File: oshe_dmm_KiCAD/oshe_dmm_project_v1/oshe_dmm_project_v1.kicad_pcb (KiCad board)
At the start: 4 copper layers, 101.6 x 177.8 mm, 55 parts, among them J1 FTDI Basic, J2 USB_C_Receptacle_PowerOnly_6P, J3 ON/OFF, SW1 SW_Push, U1 ATmega328P-A, U2 INA219BxD, U3 BQ24075RGT, U4 LM317_SOT-223, Y1 16MHz

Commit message: More changes plus custom footprints and symbols!
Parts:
- added F1: 5A, Fuse:Fuseholder_Clip-5x20mm_Keystone_3512P_Inline_P23.62x7.27mm_D1.02x2.41x1.02x1.57mm_Horizontal, F.Cu at (176.8, 235.1)
- F2: renamed from F1; value Fuse -> 500mA
- SW1: value SW_Push -> PTS526 SK15 SMTR2 LFS; footprint Button_Switch_SMD:SW_Push_1P1T-MP_NO_Horizontal_Alps_SKRTLAE010 -> DMM_Footprint_Library:SMT_FS
- moved D1 8.52 mm to (189.3, 217.0)
- moved R2 8.52 mm to (190.8, 206.8)
- moved R3 8.52 mm to (189.3, 210.6)
- moved SW1 8.47 mm to (131.1, 175.6)
- moved F2 8.26 mm to (197.9, 223.3)
- moved R1 2.67 mm to (170.8, 232.8)
- moved R4 2.67 mm to (154.5, 232.5)
- moved C2 2.67 mm to (166.5, 235.6)
- moved R5 2.67 mm to (154.5, 230.1)
- moved U2 2.67 mm to (161.4, 233.1)
- renumbered C10 to C12, C11 to C13, C12 to C15, C13 to C16, R2 to R1, R9 to R14, R10 to R15, R11 to R16, R12 to R19, R1 to R2, R14 to R20, R13 to R21, R4 to R3, R3 to R4, R8 to R9, RV2 to RV1, U4 to U5
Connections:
- net Current Positive renamed Net-(U2-IN+)
- DS1 pad 15: +5V -> Net-(DS1-LED(+))
- SW1 pad 1: GND -> Net-(U1-~{RESET}/PC6)
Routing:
- net GND: track 22.2 -> 36.6 mm
- net Net-(U1-~{RESET}/PC6): track 49.0 -> 59.4 mm

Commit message: Friday Library Meeting
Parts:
- added C14: 100nF, Capacitor_SMD:C_1206_3216Metric_Pad1.33x1.80mm_HandSolder, F.Cu at (94.3, 133.3)
- added D6: SMAJ200CA, Diode_SMD:D_SMA, F.Cu at (79.0, 114.3)
- added J4: Voltage, DMM_Footprint_Library:CONN_575-8_KEY, F.Cu at (207.5, 192.3)
- added J5: GND, DMM_Footprint_Library:CONN_575-8_KEY, F.Cu at (207.5, 211.3)
- added J6: Current, DMM_Footprint_Library:CONN_575-8_KEY, F.Cu at (207.5, 230.3)
- added R10: 900K, Resistor_SMD:R_1206_3216Metric_Pad1.30x1.75mm_HandSolder, F.Cu at (192.9, 151.2)
- added R11: 90k, Resistor_SMD:R_1206_3216Metric_Pad1.30x1.75mm_HandSolder, F.Cu at (192.9, 156.6)
- added R13: 10k, Resistor_SMD:R_1206_3216Metric_Pad1.30x1.75mm_HandSolder, F.Cu at (192.9, 162.0)
- added R22: 10k, Resistor_SMD:R_1206_3216Metric_Pad1.30x1.75mm_HandSolder, F.Cu at (100.8, 129.0)
- added R23: 10k, Resistor_SMD:R_1206_3216Metric_Pad1.30x1.75mm_HandSolder, F.Cu at (100.8, 131.4)
- added R8: 220K, Resistor_SMD:R_1206_3216Metric_Pad1.30x1.75mm_HandSolder, F.Cu at (127.4, 138.1)
- added U6: ADS1115IDGS, Package_SO:TSSOP-10_3x3mm_P0.5mm, F.Cu at (89.0, 131.8)
- moved F2 40.3 mm to (207.5, 184.2)
- moved F1 19.8 mm to (196.6, 234.9), turned to 180 degrees
- moved C2 7.38 mm to (167.0, 228.3)
- moved R5 7.38 mm to (155.0, 222.7)
- moved U2 7.38 mm to (161.9, 225.7)
- moved R1 7.38 mm to (171.3, 225.5)
- moved R4 7.38 mm to (155.0, 225.1)
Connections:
- net Current Negative renamed Input_Negative
- F1 pad 1: Current Positive -> Current_Input
- F2 pad 1: Net-(F2-Pad1) -> Voltage_Input
- F2 pad 2: Net-(F2-Pad2) -> /2V
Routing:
- net /2V: track 0.00 -> 29.8 mm
- net Voltage_Input: track 0.00 -> 8.10 mm
- net (no net): vias 0 -> 1
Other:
- outline, holes or cut-outs redrawn

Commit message: Replaced PCB file with update
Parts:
- moved R10 3.40 mm to (196.3, 151.5)
- moved R11 3.40 mm to (196.3, 156.9)
- moved R13 3.40 mm to (196.3, 162.4)
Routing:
- net /2V: track 29.8 -> 31.3 mm
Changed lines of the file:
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@@
 		(fp_arc
 			(start 64.20104 22.49932)
-			(mid 64.054473 22.853115)
+			(mid 64.054479 22.85315)
 			(end 63.70066 22.9997)
 			(stroke
@@
 	(footprint "Resistor_SMD:R_1206_3216Metric_Pad1.30x1.75mm_HandSolder"
 		(layer "F.Cu")
-		(at 192.93 162.048 -90)
+		(at 196.315 162.389 -90)
 		(descr "Resistor SMD 1206 (3216 Metric), square (rectangular) end terminal, IPC_7351 nominal with elongated pad for handsoldering. (Body size source: IPC-SM-782 page 72, https://www.pcb-3d.com/wordpress/wp-content/uploads/ipc-sm-782a_amendment_1_and_2.pdf), generated with kicad-footprint-generator")
 		(tags "resistor handsolder")
@@
 		(tags "resistor handsolder")
 		(property "Reference" "R23"
-			(at -3.937 0 360)
+			(at -3.937 0 0)
 			(layer "F.SilkS")
 			(effects
@@
 		)
 		(property "Value" "10k"
-			(at 0 1.82 360)
+			(at 0 1.82 0)
 			(layer "F.Fab")
 			(effects
@@
 		)
 		(fp_text user "${REFERENCE}"
-			(at 0 0 360)
+			(at 0 0 0)
 			(layer "F.Fab")
 			(effects
@@
 		(tags "fuse clip open")
 		(property "Reference" "F1"
-			(at 11.81 -4.5 360)
+			(at 11.81 -4.5 0)
 			(layer "F.SilkS")
 			(effects
@@
 		)
 		(property "Value" "5A"
-			(at 11.555 4.5 360)
+			(at 11.555 4.5 0)
 			(layer "F.Fab")
 			(effects
@@
 		)
 		(fp_text user "${REFERENCE}"
-			(at 11.81 0 360)
+			(at 11.81 0 0)
 			(layer "F.Fab")
 			(effects
@@
 	(footprint "Resistor_SMD:R_1206_3216Metric_Pad1.30x1.75mm_HandSolder"
 		(layer "F.Cu")
-		(at 192.93 151.15 -90)
+		(at 196.315 151.491 -90)
 		(descr "Resistor SMD 1206 (3216 Metric), square (rectangular) end terminal, IPC_7351 nominal with elongated pad for handsoldering. (Body size source: IPC-SM-782 page 72, https://www.pcb-3d.com/wordpress/wp-content/uploads/ipc-sm-782a_amendment_1_and_2.pdf), generated with kicad-footprint-generator")
 		(tags "resistor handsolder")
@@
 	(footprint "Resistor_SMD:R_1206_3216Metric_Pad1.30x1.75mm_HandSolder"
 		(layer "F.Cu")
-		(at 192.93 156.587 -90)
+		(at 196.315 156.928 -90)
 		(descr "Resistor SMD 1206 (3216 Metric), square (rectangular) end terminal, IPC_7351 nominal with elongated pad for handsoldering. (Body size source: IPC-SM-782 page 72, https://www.pcb-3d.com/wordpress/wp-content/uploads/ipc-sm-782a_amendment_1_and_2.pdf), generated with kicad-footprint-generator")
 		(tags "resistor handsolder")
@@
 		(tags "resistor handsolder")
 		(property "Reference" "R22"
-			(at -3.937 0 360)
+			(at -3.937 0 0)
 			(layer "F.SilkS")
 			(effects
@@
 		)
 		(property "Value" "10k"
-			(at 0 1.82 360)
+			(at 0 1.82 0)
 			(layer "F.Fab")
 			(effects
@@
 		)
 		(fp_text user "${REFERENCE}"
-			(at 0 0 360)
+			(at 0 0 0)
 			(layer "F.Fab")
 			(effects
@@
 	(gr_circle
 		(center 164.49 152.078)
-		(end 174.49 152.078)
+		(end 189.490112 152.078)
 		(stroke
 			(width 2)
@@
 	(gr_circle
 		(center 164.49 152.078)
-		(end 179.49 152.078)
+		(end 174.49 152.078)
 		(stroke
 			(width 2)
@@
 	(gr_circle
 		(center 164.49 152.078)
-		(end 184.49 152.078)
+		(end 179.49 152.078)
 		(stroke
 			(width 2)
@@
 		(layer "F.Cu")
 	)
+	(gr_arc
+		(start 171.355591 133.293334)
+		(mid 174.515111 134.772014)
+		(end 177.36964 136.777187)
+		(stroke
+			(width 2)
+			(type default)
+		)
+		(layer "F.Cu")
+	)
+	(gr_arc
+		(start 184.19146 148.63527)
+		(mid 184.489977 152.107139)
+		(end 184.181345 155.578124)
+		(stroke
+			(width 2)
+			(type default)
+		)
+		(layer "F.Cu")
+	)
+	(gr_arc
+		(start 179.834186 139.250063)
+		(mid 181.825381 142.103805)
+		(end 183.291804 145.259484)
+		(stroke
+			(width 2)
+			(type default)
+		)
+		(layer "F.Cu")
+	)
 	(gr_line
 		(start 148.488 240.47)
@@
 	)
 	(gr_arc
-		(start 150.389743 146.959687)
-		(mid 151.493044 144.58844)
-		(end 152.991432 142.444865)
+		(start 171.355591 133.293334)
+		(mid 174.515111 134.772014)
+		(end 177.36964 136.777187)
 		(stroke
-			(width 0.1)
+			(width 2)
 			(type default)
 		)
@@
 	)
 	(gr_arc
-		(start 167.092897 137.305071)
-		(mid 167.734534 137.432608)
-		(end 168.37 137.588)
+		(start 164.49 132.078)
+		(mid 166.238117 132.154544)
+		(end 167.972853 132.383591)
 		(stroke
 			(width 0.5)
@@
 	)
 	(gr_arc
-		(start 154.840216 140.593398)
-		(mid 156.983677 139.090717)
-		(end 159.355732 137.983544)
+		(start 167.972853 132.383591)
+		(mid 169.684178 132.764261)
+		(end 171.355591 133.293334)
 		(stroke
-			(width 0.1)
+			(width 0.5)
 			(type default)
 		)
@@
 	)
 	(gr_arc
-		(start 174.127591 140.583164)
-		(mid 175.090932 141.465053)
-		(end 175.973912 142.427394)
+		(start 168.37 137.588)
+		(mid 164.495001 167.078482)
+		(end 160.600343 137.59059)
 		(stroke
-			(width 0.5)
+			(width 2)
 			(type default)
 		)
@@
 	)
 	(gr_arc
-		(start 152.991431 142.444864)
-		(mid 153.875378 141.478745)
-		(end 154.840216 140.593398)
+		(start 168.837468 127.458911)
+		(mid 170.975549 127.933898)
+		(end 173.063852 128.594196)
 		(stroke
 			(width 0.5)
@@
 	)
 	(gr_arc
-		(start 168.37 137.588)
-		(mid 168.998655 137.77113)
-		(end 169.618719 137.981521)
+		(start 167.08526 142.420641)
+		(mid 167.505215 142.543409)
+		(end 167.919399 142.684428)
 		(stroke
-			(width 0.5)
+			(width 0.1)
 			(type default)
 		)
@@
 	)
 	(gr_arc
-		(start 178.582584 146.938592)
-		(mid 178.977173 148.187465)
-		(end 179.261319 149.465998)
+		(start 173.063852 128.594197)
+		(mid 186.151091 139.59613)
+		(end 189.107234 156.435951)
 		(stroke
-			(width 0.5)
+			(width 2)
 			(type default)
 		)
@@
 	)
 	(gr_arc
-		(start 161.884844 137.30547)
-		(mid 164.488853 137.077517)
-		(end 167.092897 137.305071)
+		(start 151.642701 136.750023)
+		(mid 154.496384 134.753809)
+		(end 157.653083 133.28288)
 		(stroke
 			(width 0.1)
@@
 	)
 	(gr_arc
-		(start 179.261318 149.465998)
-		(mid 179.490478 152.070528)
-		(end 179.263913 154.675286)
+		(start 184.19146 148.63527)
+		(mid 184.489977 152.107139)
+		(end 184.181345 155.578124)
+		(stroke
+			(width 2)
+			(type default)
+		)
+		(layer "F.Mask")
+	)
+	(gr_arc
+		(start 161.030142 132.379539)
+		(mid 162.753513 132.153527)
+		(end 164.49 132.078)
+		(stroke
+			(width 0.5)
+			(type default)
+		)
+		(layer "F.Mask")
+	)
+	(gr_arc
+		(start 179.834186 139.250063)
+		(mid 181.825381 142.103805)
+		(end 183.291804 145.259484)
+		(stroke
+			(width 2)
+			(type default)
+		)
+		(layer "F.Mask")
+	)
+	(gr_arc
+		(start 145.693403 145.245149)
+		(mid 147.169742 142.07757)
+		(end 149.174918 139.215333)
 		(stroke
 			(width 0.1)
@@
 	)
 	(gr_arc
-		(start 159.355732 137.983543)
-		(mid 159.973762 137.773525)
-		(end 160.600343 137.590592)
+		(start 157.653083 133.28288)
+		(mid 159.321838 132.757284)
+		(end 161.030142 132.37954)
 		(stroke
 			(width 0.5)
@@
 	)
 	(gr_arc
-		(start 169.618719 137.981522)
-		(mid 171.986874 139.085258)
-		(end 174.127592 140.583163)
+		(start 167.919399 142.684429)
+		(mid 164.486833 162.077995)
+		(end 161.066551 142.682259)
 		(stroke
-			(width 0.1)
+			(width 2)
 			(type default)
 		)
@@
 	)
 	(gr_arc
-		(start 160.600343 137.590591)
-		(mid 161.239466 137.433941)
-		(end 161.884844 137.305471)
+		(start 149.174918 139.215333)
+		(mid 150.35496 137.928774)
+		(end 151.642701 136.750023)
 		(stroke
 			(width 0.5)
@@
 	)
 	(gr_arc
-		(start 175.973912 142.427394)
-		(mid 177.475646 144.568844)
-		(end 178.582584 146.938592)
+		(start 164.49 127.078)
+		(mid 166.672062 127.17341)
+		(end 168.837468 127.458911)
 		(stroke
-			(width 0.1)
+			(width 0.5)
 			(type default)
 		)
@@
 	)
 	(segment
+		(start 209.054 162.803)
+		(end 185.739 162.803)
+		(width 0.2)
+		(layer "B.Cu")
+		(net 60)
+	)
+	(segment
 		(start 180.48 160.588)
 		(end 178.569264 158.677264)
@@
 	)
 	(segment
-		(start 207.543 160.588)
-		(end 180.48 160.588)
+		(start 210.928 160.929)
+		(end 209.054 162.803)
+		(width 0.2)
+		(layer "B.Cu")
+		(net 60)
+	)
+	(segment
+		(start 185.739 162.803)
+		(end 183.865 160.929)
 		(width 0.2)
 		(layer "B.Cu")

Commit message: updated
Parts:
- moved R10 3.31 mm to (198.5, 149.0)
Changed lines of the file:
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@@
 		(fp_arc
 			(start 64.20104 22.49932)
-			(mid 64.054479 22.85315)
+			(mid 64.054473 22.853115)
 			(end 63.70066 22.9997)
 			(stroke
@@
 	(footprint "Resistor_SMD:R_1206_3216Metric_Pad1.30x1.75mm_HandSolder"
 		(layer "F.Cu")
-		(at 196.315 151.491 -90)
+		(at 198.465 148.978 -90)
 		(descr "Resistor SMD 1206 (3216 Metric), square (rectangular) end terminal, IPC_7351 nominal with elongated pad for handsoldering. (Body size source: IPC-SM-782 page 72, https://www.pcb-3d.com/wordpress/wp-content/uploads/ipc-sm-782a_amendment_1_and_2.pdf), generated with kicad-footprint-generator")
 		(tags "resistor handsolder")

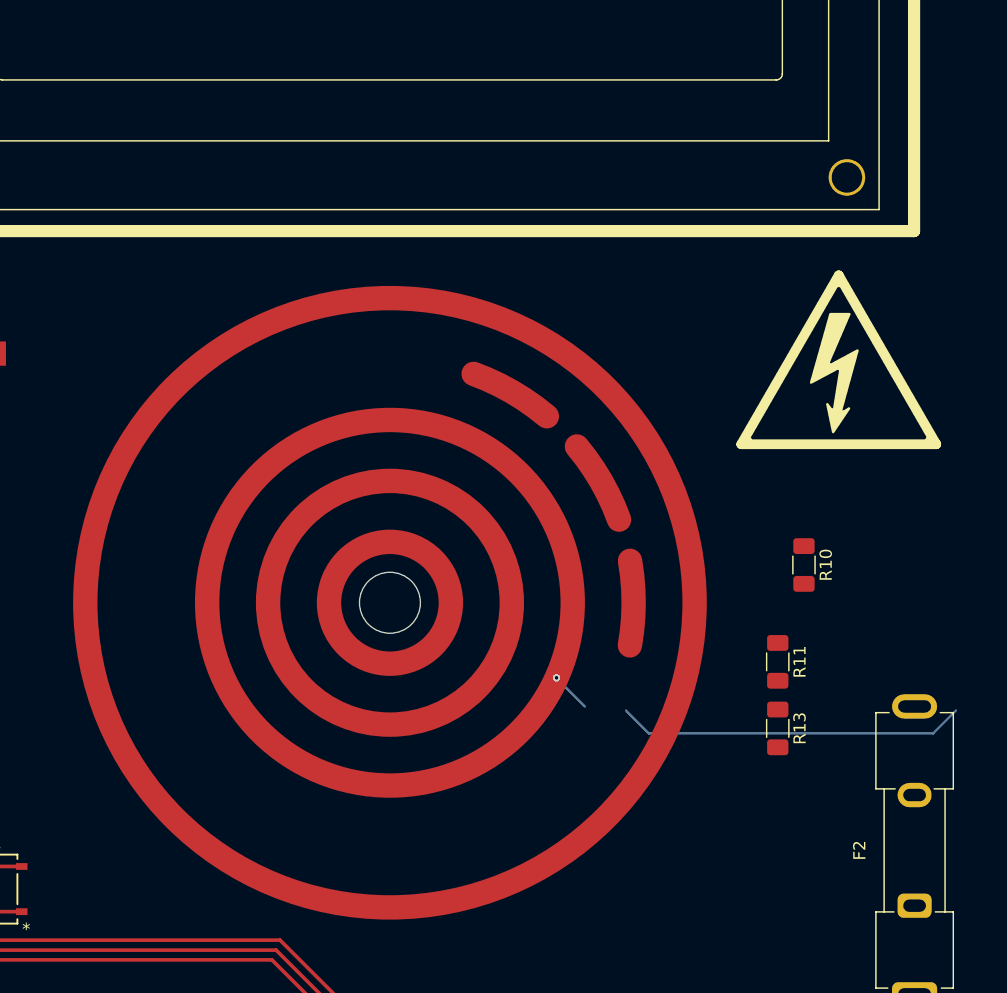
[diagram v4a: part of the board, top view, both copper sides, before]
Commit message: Updated Switch
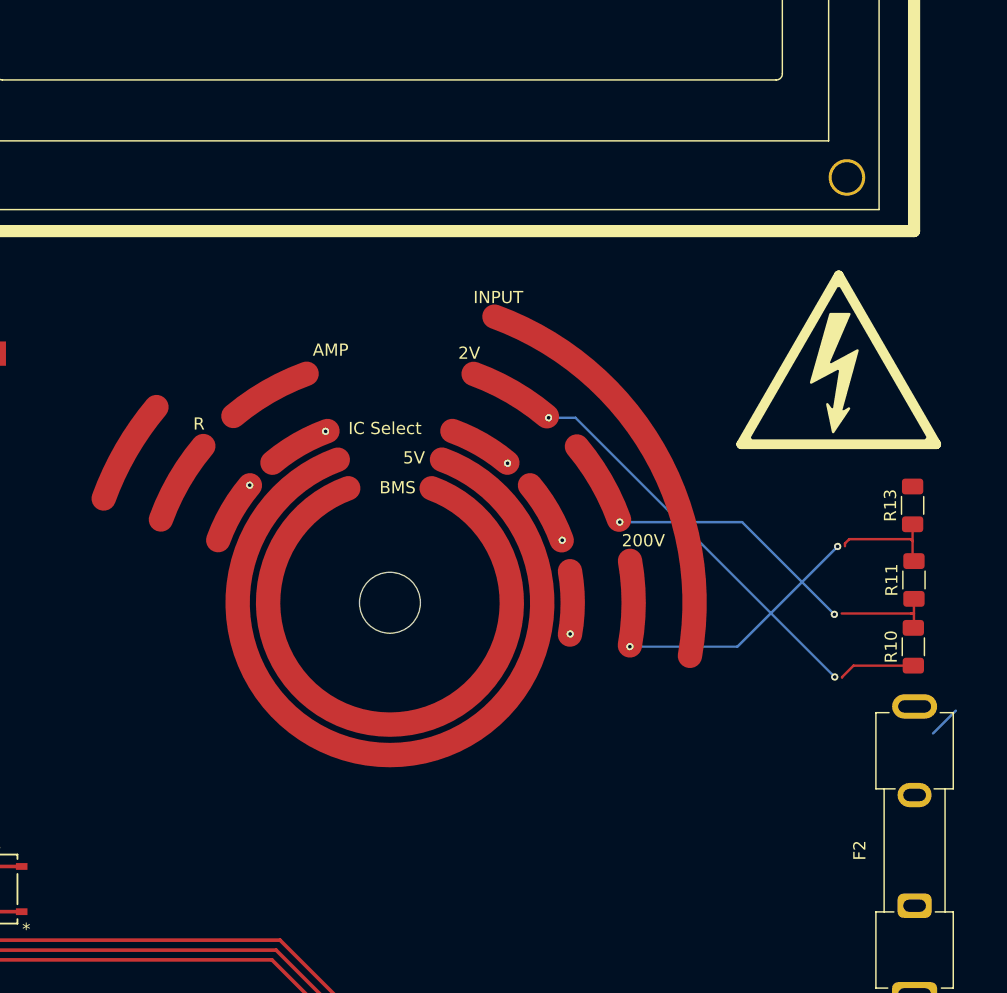
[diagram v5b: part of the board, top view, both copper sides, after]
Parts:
- moved R13 21.4 mm to (207.4, 144.1), turned to 90 degrees
- moved R11 13.0 mm to (207.5, 150.2), turned to 90 degrees
- moved R10 11.2 mm to (207.4, 155.7), turned to 90 degrees
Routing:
- net (no net): track 0.00 -> 73.5 mm, vias 1 -> 11
- net /2V: track 31.3 -> 8.93 mm
- net /200V: track 0.00 -> 9.06 mm
- net /20V: track 0.00 -> 8.33 mm
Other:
- board text added: "200V"
- board text added: "20V"
- board text added: "2V"
- board text added: "AMP"
- board text added: "BMS"
- board text added: "IC Select"
- board text added: "INPUT"
- board text added: "R"

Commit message: Made some updates
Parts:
- removed C14: 100nF, Capacitor_SMD:C_1206_3216Metric_Pad1.33x1.80mm_HandSolder
- removed the D1 at (189.3, 217.0)
- removed the R2 at (190.8, 206.8)
- added C11: 0.1uF, Capacitor_SMD:C_1206_3216Metric_Pad1.33x1.80mm_HandSolder, F.Cu at (181.6, 197.7)
- added J10: Voltage Range 2, Connector_PinHeader_2.54mm:PinHeader_1x02_P2.54mm_Vertical, F.Cu at (202.5, 136.5)
- added J11: Voltage Range 3, Connector_PinHeader_2.54mm:PinHeader_1x02_P2.54mm_Vertical, F.Cu at (197.8, 144.6)
- added J12: Voltage Range 3, Connector_PinHeader_2.54mm:PinHeader_1x02_P2.54mm_Vertical, F.Cu at (202.5, 144.6)
- added J13: Current, Connector_PinHeader_2.54mm:PinHeader_1x02_P2.54mm_Vertical, F.Cu at (197.9, 152.8)
- added J14: Resistance, Connector_PinHeader_2.54mm:PinHeader_1x02_P2.54mm_Vertical, F.Cu at (197.9, 161.3)
- added J15: Resistance, Connector_PinHeader_2.54mm:PinHeader_1x02_P2.54mm_Vertical, F.Cu at (202.6, 161.3)
- added J7: Voltage Range 1, Connector_PinHeader_2.54mm:PinHeader_1x02_P2.54mm_Vertical, F.Cu at (197.8, 128.3)
- added J8: Voltage Range 1, Connector_PinHeader_2.54mm:PinHeader_1x02_P2.54mm_Vertical, F.Cu at (202.5, 128.3)
- added J9: Voltage Range 2, Connector_PinHeader_2.54mm:PinHeader_1x02_P2.54mm_Vertical, F.Cu at (197.8, 136.5)
- added R10: 1k, Resistor_SMD:R_1206_3216Metric_Pad1.30x1.75mm_HandSolder, F.Cu at (179.7, 186.5)
- added R4: 1k, Resistor_SMD:R_1206_3216Metric_Pad1.30x1.75mm_HandSolder, F.Cu at (169.8, 186.5)
- added R5: 1k, Resistor_SMD:R_1206_3216Metric_Pad1.30x1.75mm_HandSolder, F.Cu at (173.1, 186.5)
- added R9: 1k, Resistor_SMD:R_1206_3216Metric_Pad1.30x1.75mm_HandSolder, F.Cu at (176.4, 186.5)
- R3: value 10k -> 1k
- moved D2 148.3 mm to (198.8, 201.7), turned to -90 degrees
- moved U5 115.2 mm to (184.9, 195.6), turned to -90 degrees
- moved R22 113.0 mm to (186.8, 202.3), turned to 90 degrees
- moved R23 109.6 mm to (184.4, 202.3), turned to 90 degrees
- moved REF** 81.8 mm to (263.2, 78.7)
- moved R14 49.5 mm to (193.1, 203.0)
- moved R15 49.5 mm to (193.1, 197.5)
- moved R16 49.5 mm to (193.0, 191.4)
- moved R3 33.1 mm to (166.5, 186.5)
- moved R7 32.2 mm to (186.8, 218.2), turned to -90 degrees
- moved R2 30.3 mm to (183.8, 215.8), turned to -90 degrees
- moved R1 28.6 mm to (199.5, 220.8), turned to 90 degrees
- moved U2 21.0 mm to (182.7, 222.3), turned to -90 degrees
- moved C3 12.4 mm to (178.5, 223.6), turned to 90 degrees
- moved R11 10.7 mm to (136.4, 132.3), turned to 90 degrees
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- renumbered C13 to C10, C15 to C12, C16 to C13, C3 to C2, C2 to C3, C5 to C4, C6 to C5, C7 to C6, C8 to C7, C9 to C8, C12 to C9, D2 to D1, D6 to D2, D3 to D4, D4 to D5, J4 to J2, J5 to J3, J6 to J4, J2 to J5, J3 to J6, R8 to R11, R9 to R12, R14 to R13, R10 to R14, R11 to R15, R13 to R16, R15 to R17, R16 to R18, R4 to R2, R5 to R7, R7 to R8, U5 to U4, U6 to U5
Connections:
- net /200V renamed 200V_Rang
- net /20V renamed 20V_Rang
- D2 pad 1: Input_Negative -> 2V_Rang
- D2 pad 2: /2V -> Input_Negative
- F2 pad 2: /2V -> 2V_Rang
- R14 pad 1: /2V -> 2V_Rang
- R3 pad 1: Net-(D1-A2) -> A3
- U5 pad 4: Net-(D5-A2) -> V_ADC_Input
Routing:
- net GND: track 36.6 -> 141.0 mm
- net +5V: track 20.4 -> 101.7 mm
- net (no net): track 73.5 -> 0.00 mm, vias 11 -> 8
- net Net-(DS1-LED(+)): track 0.00 -> 57.6 mm
- net Net-(DS1-VO): track 0.00 -> 47.9 mm
- net A3: track 0.00 -> 17.3 mm
- net /2V: track 8.93 -> 0.00 mm
- net Voltage_Input: track 8.10 -> 0.00 mm
- net TXD: track 48.5 -> 41.5 mm
- net RXD: track 50.6 -> 43.6 mm
- net 200V_Rang: track 9.06 -> 3.07 mm
- net 20V_Rang: track 8.33 -> 2.62 mm
- net SCL: track 0.00 -> 3.25 mm
- net SDA: track 0.00 -> 3.24 mm
- net Net-(U2-A0): track 0.00 -> 2.84 mm
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- added copper zone on F.Cu, net Net-(D4-A)
- removed copper zone on F.Cu, net Net-(D5-A)
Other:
- board text added: "ADC INPUT"
- board text removed: "INPUT"
